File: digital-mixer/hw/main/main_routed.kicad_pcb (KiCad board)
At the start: 4 copper layers, 104.5 x 136.5 mm, 190 parts, among them J1 GCT USB4110-GF-A, J10 MIDI OUT SJ-43514-SMT, J2 LiPo 1S 3000 mAh (з платою за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, J3 IN1 SJ-43514-SMT, J4 IN2 SJ-43514-SMT, J5 IN3 SJ-43514-SMT, J6 IN4 SJ-43514-SMT, J7 MAIN OUT SJ-43514-SMT, J8 AUX OUT SJ-43514-SMT, J9 PHONES SJ-43514-SMT, Q1 AO3401A, SW1 Power 5.8mm DPDT self-lock SMD, SW10 EC12SY ch3.1, SW11 EC12SY ch3.2, SW12 EC12SY ch3.3, SW13 Mute 3 TSF-1266, SW14 EC12SY ch4.1, SW15 EC12SY ch4.2, SW16 EC12SY ch4.3, SW17 Mute 4 TSF-1266, SW18 EC12SY master, SW19 FX1 TSF-1266, SW2 EC12SY ch1.1, SW20 FX2 TSF-1266, SW21 AUX TSF-1266, SW22 SHIFT TSF-1266, SW3 EC12SY ch1.2, SW4 EC12SY ch1.3, SW5 Mute 1 TSF-1266, SW6 EC12SY ch2.1, SW7 EC12SY ch2.2, SW8 EC12SY ch2.3, SW9 Mute 2 TSF-1266, U1 Teensy 4.1, U10 PCM5102A, U11 TPA6132A2, U12 MCP23017-E/SO, U13 MCP23017-E/SO, U14 MCP23017-E/SO, U2 USBLC6-2SC6, U3 TP4056, U4 TPS63802, U5 LP5907MFX-3.3, U6 PCM1865, U7 PCM1865, U8 PCM5102A, U9 PCM5102A

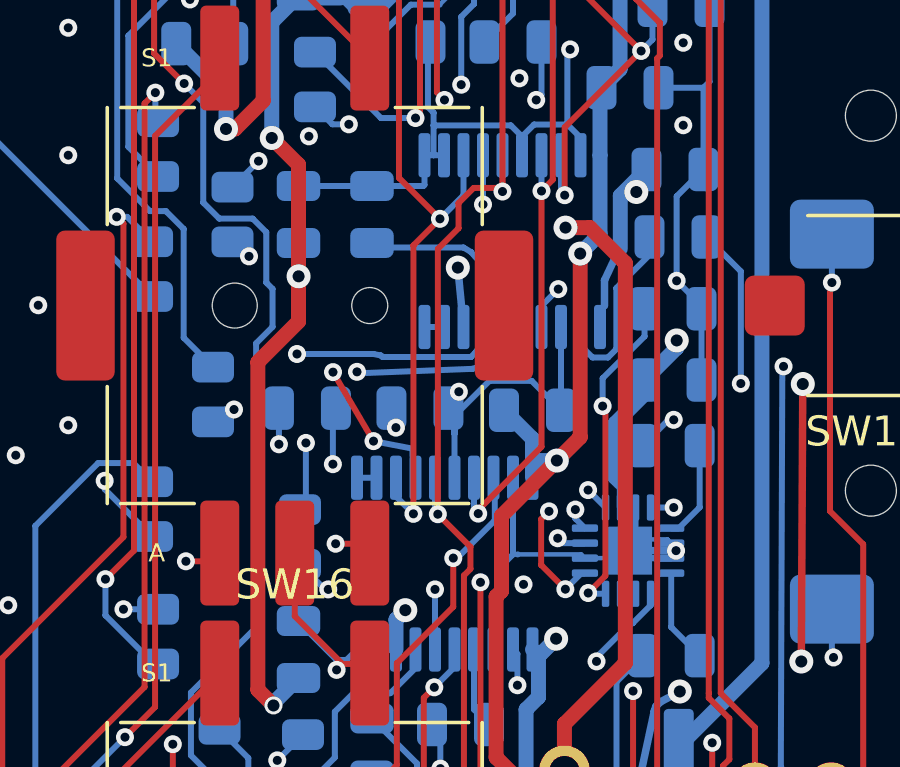
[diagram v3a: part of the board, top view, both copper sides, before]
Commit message: digital-mixer: перевірка перед замовленням (07-review): +3V3A у межах LP5907 (DM37), переходи з площадок, дроти USB Teensy, USB-живлення в прошивці
Co-Authored-By: Claude Opus 5.5 <noreply@anthropic.com>
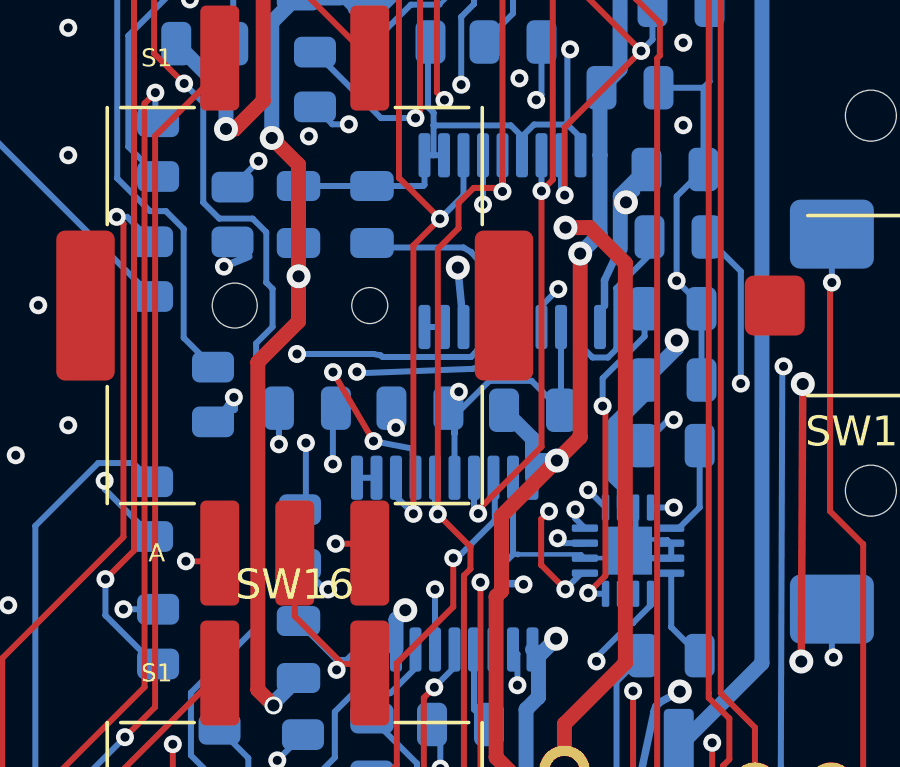
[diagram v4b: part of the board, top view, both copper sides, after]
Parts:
- C11: value 10u -> 2.2u
- C18, C30, C41, C52, C63: value 10u -> 1u
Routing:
- net /AUX_OR: track 9.60 -> 11.7 mm
- net /+3V3A: track 318.8 -> 320.8 mm
- net /AUX_OL: track 10.4 -> 12.2 mm
- net /GND: track 561.4 -> 560.3 mm, vias 496 -> 495
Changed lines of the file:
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@@
 			)
 		)
-		(property "Value" "10u"
+		(property "Value" "1u"
 			(at 0 -1.85 180)
 			(layer "B.Fab")
@@
 			)
 		)
-		(property "Value" "10u"
+		(property "Value" "2.2u"
 			(at 0 -1.85 180)
 			(layer "B.Fab")
@@
 			)
 		)
-		(property "Value" "10u"
+		(property "Value" "1u"
 			(at 0 -1.85 180)
 			(layer "B.Fab")
@@
 			)
 		)
-		(property "Value" "10u"
+		(property "Value" "1u"
 			(at 0 -1.85 180)
 			(layer "B.Fab")
@@
 			)
 		)
-		(property "Value" "10u"
+		(property "Value" "1u"
 			(at 0 -1.85 180)
 			(layer "B.Fab")
@@
 			)
 		)
-		(property "Value" "10u"
+		(property "Value" "1u"
 			(at 0 -1.85 180)
 			(layer "B.Fab")
@@
 	)
 	(via
-		(at 105.21 83.13)
-		(size 0.6)
-		(drill 0.3)
-		(layers "F.Cu" "B.Cu")
-		(net "/GND")
-	)
-	(via
 		(at 40.7 104.95)
 		(size 0.6)
@@
 	)
 	(segment
+		(start 99.326 84.23)
+		(end 99.826 84.23)
+		(width 0.25)
+		(layer "B.Cu")
+		(net "/GND")
+	)
+	(segment
 		(start 106.06 74.9646)
 		(end 106.06 75.0675)
@@
 	)
 	(segment
-		(start 103.61 83.13)
-		(end 105.21 83.13)
-		(width 0.25)
-		(layer "B.Cu")
-		(net "/GND")
-	)
-	(segment
 		(start 66.537 123.798)
 		(end 66.5499 123.798)
@@
 	)
 	(via
-		(at 90.975 73.32)
+		(at 90.14 73.66)
 		(size 0.6)
 		(drill 0.3)
@@
 	)
 	(segment
+		(start 90.97 73.32)
+		(end 90.14 73.66)
+		(width 0.25)
+		(layer "B.Cu")
+		(net "/AUX_OL")
+	)
+	(segment
 		(start 94.575 77.17)
 		(end 90.975 73.32)
@@
 		(net "/AUX_OL")
 	)
+	(segment
+		(start 90.975 73.32)
+		(end 90.14 73.66)
+		(width 0.25)
+		(layer "In2.Cu")
+		(net "/AUX_OL")
+	)
 	(via
 		(at 104.455 63.7486)
@@
 	)
 	(via
-		(at 103.885 71.175)
+		(at 103.54 71.52)
 		(size 0.8)
 		(drill 0.4)
@@
 	)
 	(segment
+		(start 103.885 71.175)
+		(end 103.54 71.52)
+		(width 0.25)
+		(layer "B.Cu")
+		(net "/+3V3A")
+	)
+	(segment
 		(start 104.685 88.175)
 		(end 104.535 88.325)
@@
 	)
 	(segment
+		(start 103.885 71.125)
+		(end 103.54 71.52)
+		(width 0.25)
+		(layer "B.Cu")
+		(net "/+3V3A")
+	)
+	(segment
 		(start 95.4222 64.9309)
 		(end 94.6398 64.9309)
@@
 	)
 	(segment
+		(start 103.89 71.17)
+		(end 103.54 71.52)
+		(width 0.25)
+		(layer "B.Cu")
+		(net "/+3V3A")
+	)
+	(segment
 		(start 74.525 109.638)
 		(end 74.613 109.638)
@@
 	)
 	(segment
+		(start 103.885 71.175)
+		(end 103.54 71.52)
+		(width 0.25)
+		(layer "In2.Cu")
+		(net "/+3V3A")
+	)
+	(segment
 		(start 23.1624 28.4874)
 		(end 24.2497 27.4001)
@@
 	)
 	(via
-		(at 90.475 78.425)
+		(at 90.47 78.02)
 		(size 0.6)
 		(drill 0.3)
@@
 	)
 	(segment
+		(start 90.425 78.425)
+		(end 90.47 78.02)
+		(width 0.25)
+		(layer "B.Cu")
+		(net "/AUX_OR")
+	)
+	(segment
 		(start 95.125 76.574999)
 		(end 92.574999 76.574999)
@@
 	)
 	(segment
+		(start 90.475 78.425)
+		(end 90.47 78.02)
+		(width 0.25)
+		(layer "B.Cu")
+		(net "/AUX_OR")
+	)
+	(segment
+		(start 90.47 78.42)
+		(end 90.47 78.02)
+		(width 0.25)
+		(layer "B.Cu")
+		(net "/AUX_OR")
+	)
+	(segment
+		(start 90.1875 78.425)
+		(end 90.47 78.02)
+		(width 0.25)
+		(layer "B.Cu")
+		(net "/AUX_OR")
+	)
+	(segment
 		(start 92.574999 76.574999)
 		(end 90.725 78.275)
@@
 		(layer "In2.Cu")
 		(net "/AUX_OR")
+	)
+	(segment
+		(start 90.725 78.275)
+		(end 90.47 78.02)
+		(width 0.25)
+		(layer "In2.Cu")
+		(net "/AUX_OR")
